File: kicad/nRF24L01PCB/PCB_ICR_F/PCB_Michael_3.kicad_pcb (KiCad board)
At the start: 2 copper layers, 55.9 x 58.4 mm, 2 parts, among them U1 NRF24L01_Breakout

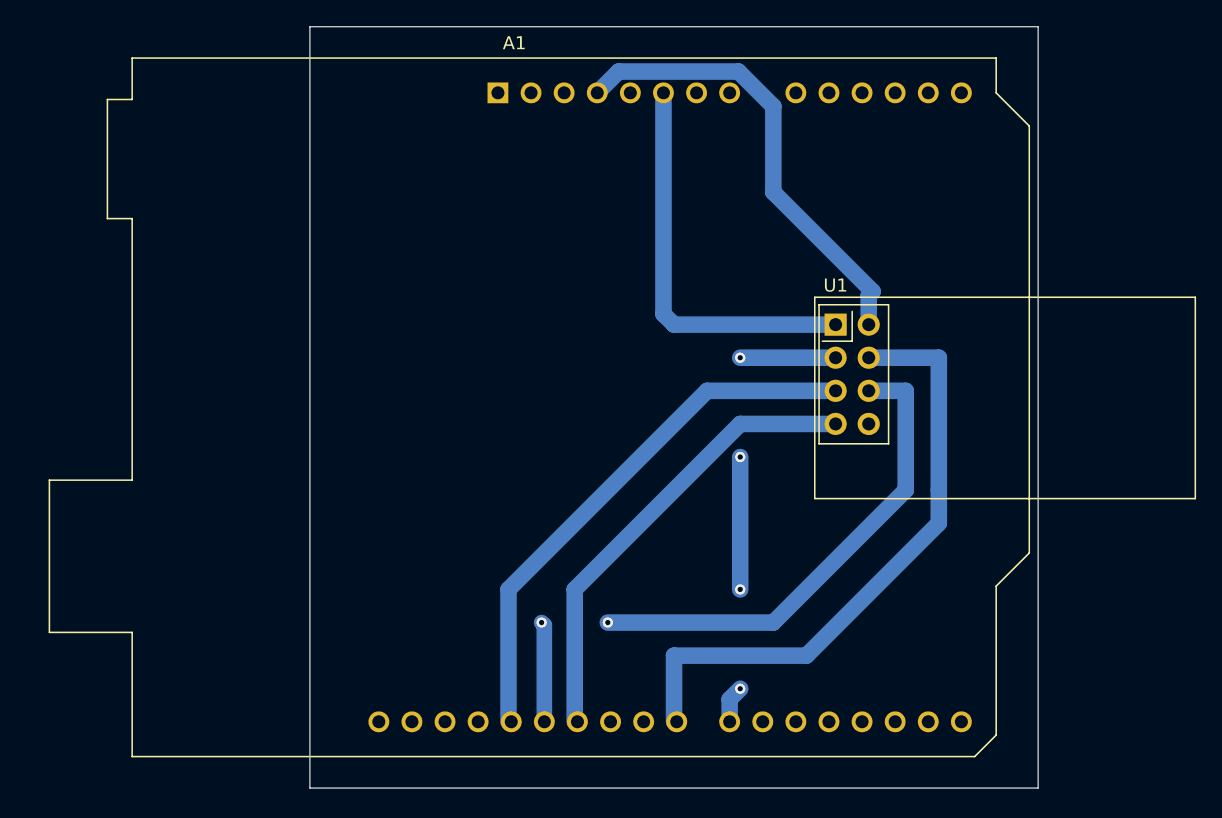
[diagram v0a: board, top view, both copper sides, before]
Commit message: 5 servo motors now!
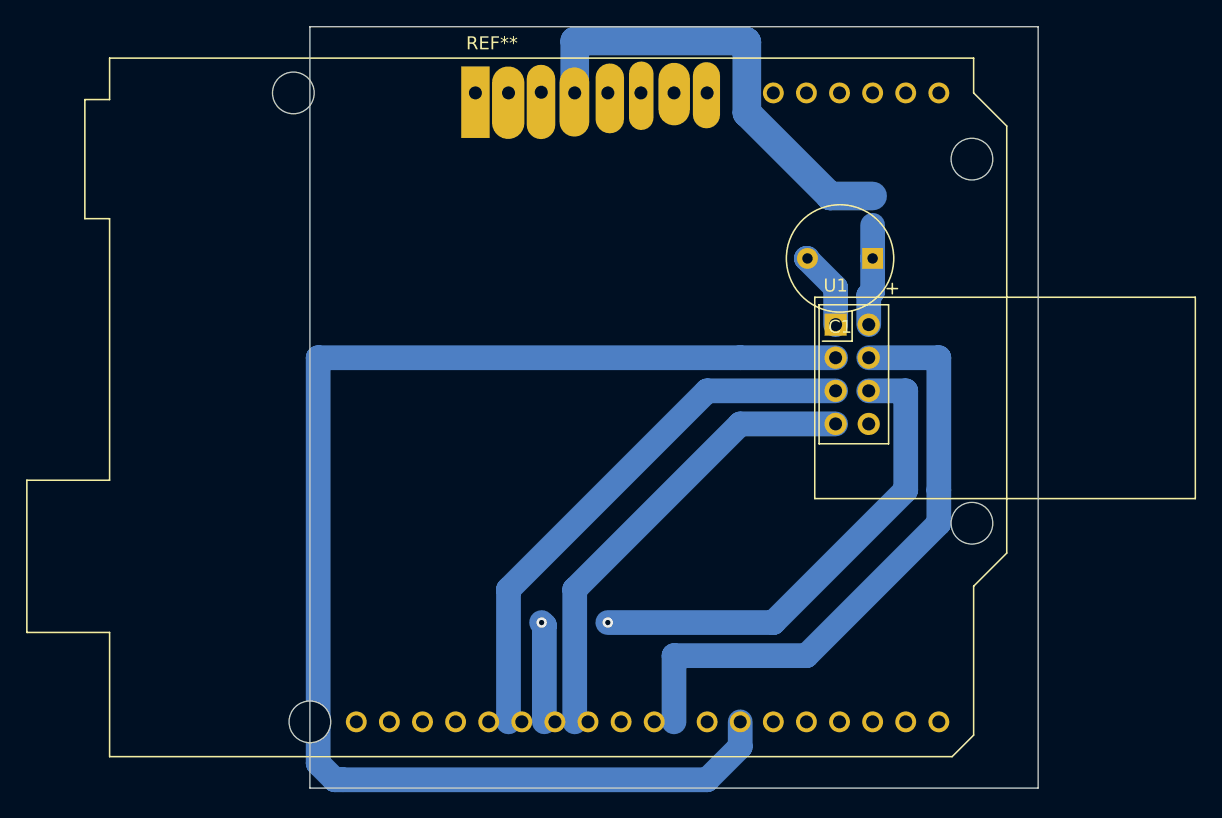
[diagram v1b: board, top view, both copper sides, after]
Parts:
- removed A1: Arduino_UNO_R3, Module:Arduino_UNO_R3
- added C1: .1 uf, Capacitor_THT:CP_Radial_Tantal_D8.0mm_P5.00mm, F.Cu at (172.7, 76.2)
- added REF**: Arduino_UNO_R3_WithMountingHoles_HugeOvalPads, myPersonalLibrary:Arduino_UNO_R3_WithMountingHoles_HugeOvalPads, F.Cu at (142.2, 63.5)
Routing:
- net Net-(A1-Pad22): track 10.2 -> 106.7 mm, vias 2 -> 0
- net Net-(A1-Pad4): track 35.3 -> 7.74 mm
- net (no net): track 10.2 -> 34.9 mm, vias 2 -> 0
- net GND: track 30.5 -> 6.09 mm
- net Net-(A1-Pad27): track 45.2 -> 37.5 mm, vias 2 -> 1
- net Net-(A1-Pad26): track 35.4 -> 43.1 mm, vias 0 -> 1
